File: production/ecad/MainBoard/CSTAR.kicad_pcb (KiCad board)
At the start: 4 copper layers, 152.4 x 152.4 mm, 180 parts, among them IC1 LT8648SEV#PBF, J1 Conn_01x02_Pin, J10 Conn_01x03_Pin, J11 B4B-PH-K-S, J12 B4B-PH-K-S, J13 Conn_01x03_Pin, J13 Conn_01x05_Pin, J14 Conn_01x03_Pin, J15 Conn_01x03_Pin, J16 Conn_01x03_Pin, J17 Ultra_4, J18 Ultra_3, J19 Ultra_2, J2 Conn_01x02_Pin, J20 RX connect, J21 Ultra_1, J22 TX connect, J23 Conn_01x02_Pin, J24 Conn_01x02_Pin, J25 TYPE-C-31-M-12, J26 532610771, J28 532610771, J29 Conn_01x04_Socket, J3 Conn_01x02_Pin, J30 691137710002, J31 TYPE-C-31-M-12, J4 XT60PW-M, J5 Conn_01x02_Pin, J6 Conn_01x02_Pin, J7 532610771, J8 Conn_01x03_Pin, J9 Conn_01x03_Pin, Q1 AO3400A, Q2 AO3400A, Q3 AO3400A, Q4 AO3400A, Q5 AO3400A, Q6 AO3400A, Q7 AO3400A, Q8 IRFHM9331TRPBF, SW1 SW_Push, SW2 SW_Push, SW3 SW_Push, SW4 SW_Push, U1 AZ1117IH-3.3TRG1, U2 DRV8842PWPR, U3 DRV8842PWPR, U4 TXB0104DR, U5 CP2102N-A01-GQFN28, U6 ESP32-WROOM-32UE_M113EH6400UH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, U7 TXB0104DR, U8 CP2102N-A01-GQFN28, U9 ESP32-WROOM-32UE_M113EH6400UH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, X1 B2P-VH, X2 B2P-VH

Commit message: "Layout Routing"
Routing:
- net GND: track 135.7 -> 204.5 mm, vias 36 -> 59
- net EN: track 0.00 -> 36.9 mm
- net +3V3: track 25.7 -> 52.0 mm, vias 2 -> 12
- net RTS: track 0.00 -> 18.3 mm
- net DTR: track 0.00 -> 17.1 mm
- net +12V: track 37.6 -> 53.0 mm, vias 5 -> 9
- net Net-(U3-VCP): track 0.00 -> 14.4 mm
- net Net-(U4-OE): track 0.00 -> 13.8 mm
- net Net-(U3-V3P3OUT): track 0.00 -> 12.1 mm
- net RGB_Red_Control: track 0.00 -> 12.0 mm
- net RGB_Green_Control: track 0.00 -> 11.9 mm
- net /CSTAR-Drive/OUT2_MOTOR_2: track 0.00 -> 9.06 mm
- net /CSTAR-Drive/OUT1_MOTOR_2: track 0.00 -> 8.95 mm
- net Net-(R16-Pad2): track 0.00 -> 8.91 mm
- net IO0: track 0.00 -> 7.18 mm
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
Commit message: "More Layout"
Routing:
- net UART_RXD: track 0.00 -> 71.8 mm, vias 0 -> 2
- net UART_TXD: track 0.00 -> 69.8 mm, vias 0 -> 2
- net 3V_echo_2: track 0.00 -> 40.1 mm, vias 0 -> 2
- net 3V_echo_3: track 0.00 -> 37.8 mm, vias 0 -> 2
- net trig_1: track 0.00 -> 36.4 mm, vias 0 -> 2
- net 3V_echo_1: track 0.00 -> 34.1 mm, vias 0 -> 2
- net 3V_echo_4: track 0.00 -> 30.3 mm, vias 0 -> 2
- net GND: track 204.5 -> 217.3 mm, vias 59 -> 63
- net IO0: track 7.18 -> 18.7 mm
- net IO0_2: track 34.2 -> 41.7 mm
- net EN_2: track 71.4 -> 78.6 mm
- net Net-(U7-OE): track 0.00 -> 6.36 mm
- net EN: track 36.9 -> 41.1 mm
- net +3.3V: track 1.24 -> 4.22 mm, vias 1 -> 3
- net +3V3: track 52.0 -> 54.5 mm, vias 12 -> 14
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
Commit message: "Even more layout"
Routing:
- net Ch.A_MOTOR_2: track 0.00 -> 187.3 mm, vias 0 -> 2
- net Ch.B_MOTOR_2: track 0.00 -> 172.7 mm, vias 0 -> 2
- net IN2_MOTOR_2: track 0.00 -> 140.5 mm, vias 0 -> 2
- net IN1_MOTOR_1: track 0.00 -> 87.6 mm, vias 0 -> 2
- net RST: track 0.00 -> 70.9 mm, vias 0 -> 2
- net GND: track 217.3 -> 277.9 mm, vias 63 -> 83
- net RXD_LIDAR: track 0.00 -> 45.2 mm
- net TXD_LIDAR: track 0.00 -> 45.2 mm
- net trig_2: track 0.00 -> 37.7 mm
- net VBUS_1: track 0.00 -> 33.2 mm, vias 0 -> 2
- net trig_4: track 0.00 -> 30.0 mm, vias 0 -> 2
- net RGB_Blue_Control: track 0.00 -> 29.9 mm, vias 0 -> 2
- net Net-(R21-Pad2): track 0.00 -> 24.4 mm, vias 0 -> 3
- net trig_3: track 0.00 -> 23.2 mm, vias 0 -> 2
- net Net-(R20-Pad2): track 0.00 -> 21.5 mm, vias 0 -> 3
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
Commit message: added gnd to make diff pairs better
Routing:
- added copper zone on In2.Cu, net GND
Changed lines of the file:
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@@
+    )
+  )
+  (zone (net 2) (net_name "GND") (layer "In2.Cu") (hatch edge 0.5)
+    (priority 7)
+    (connect_pads (clearance 0.5))
+    (min_thickness 0.25) (filled_areas_thickness no)
+    (fill yes (thermal_gap 0.5) (thermal_bridge_width 0.5))
+    (polygon
+      (pts
+        (xy 50.8 120.142)
+        (xy 68.58 120.142)
+        (xy 68.58 133.096)
+        (xy 50.8 133.096)
+      )
+    )
+  )
+  (zone (net 2) (net_name "GND") (layer "In2.Cu") (hatch edge 0.5)
+    (priority 6)
+    (connect_pads (clearance 0.5))
+    (min_thickness 0.25) (filled_areas_thickness no)
+    (fill yes (thermal_gap 0.5) (thermal_bridge_width 0.5))
+    (polygon
+      (pts
+        (xy 203.25 110.075)
+        (xy 181.775 110.025)
+        (xy 181.61 89.916)
+        (xy 203.2 89.916)
+      )
     )
   )
@@
         (xy 175.006 65.532)
         (xy 202.946 65.532)
+        (xy 203.3 89.4)
+        (xy 181.15 89.525)
+        (xy 181.125 110.475)
+        (xy 203.045432 110.475176)
         (xy 203.2 180.34)
         (xy 121.92 180.34)
@@
     (polygon
       (pts
+        (xy 50.8 133.35)
+        (xy 68.834 133.35)
+        (xy 68.834 119.888)
+        (xy 50.829297 119.887984)
         (xy 50.8 64.516)
         (xy 79.502 64.262)

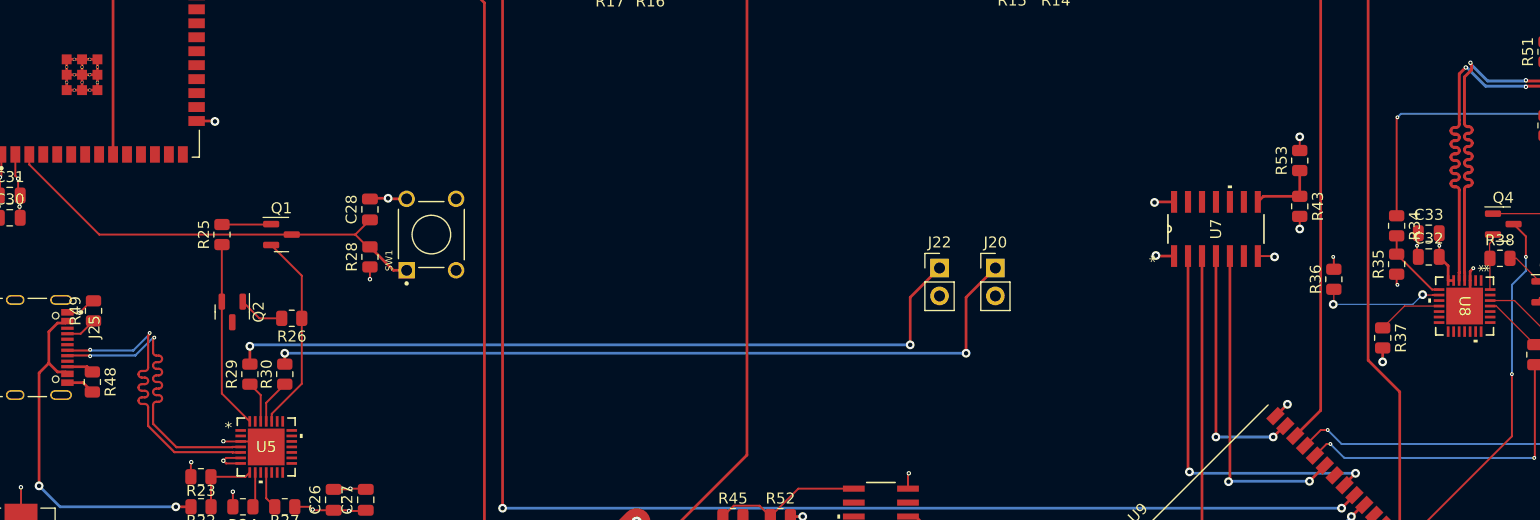
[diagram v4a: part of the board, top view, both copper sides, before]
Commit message: made my diff pairs EVEN BETTER
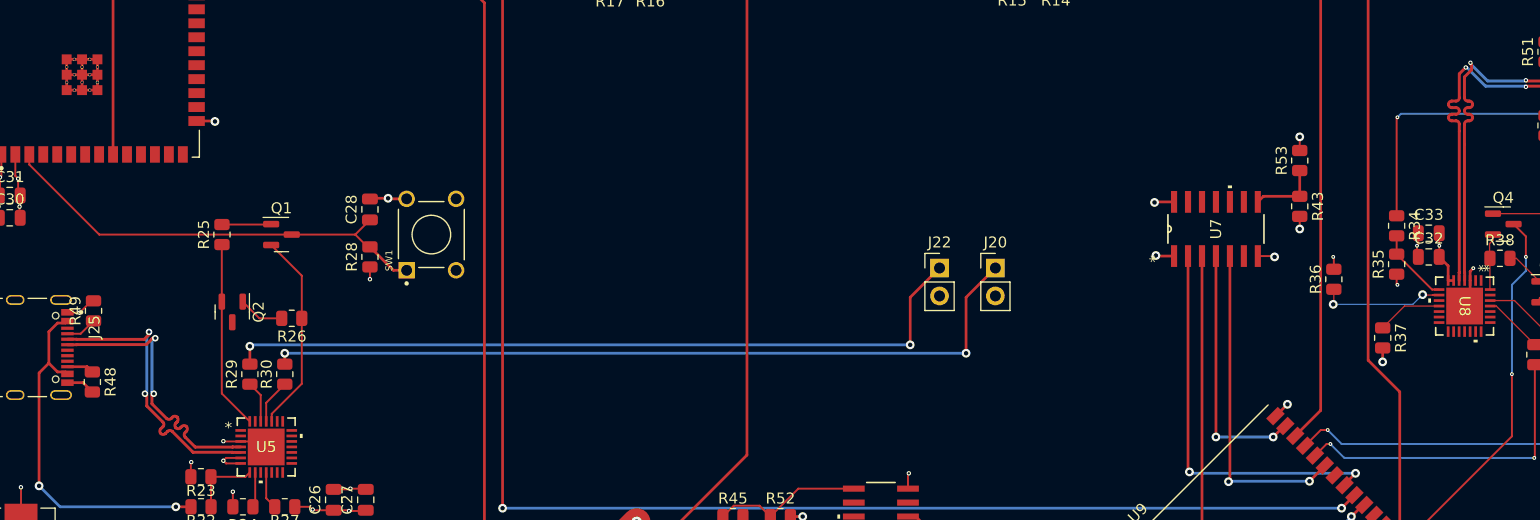
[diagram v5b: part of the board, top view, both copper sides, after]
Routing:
- net USB1_D+: track 29.7 -> 26.5 mm
- net USB1_D-: track 29.8 -> 26.6 mm
- net USB2_D+: track 37.9 -> 35.5 mm
- net USB2_D-: track 38.9 -> 36.9 mm

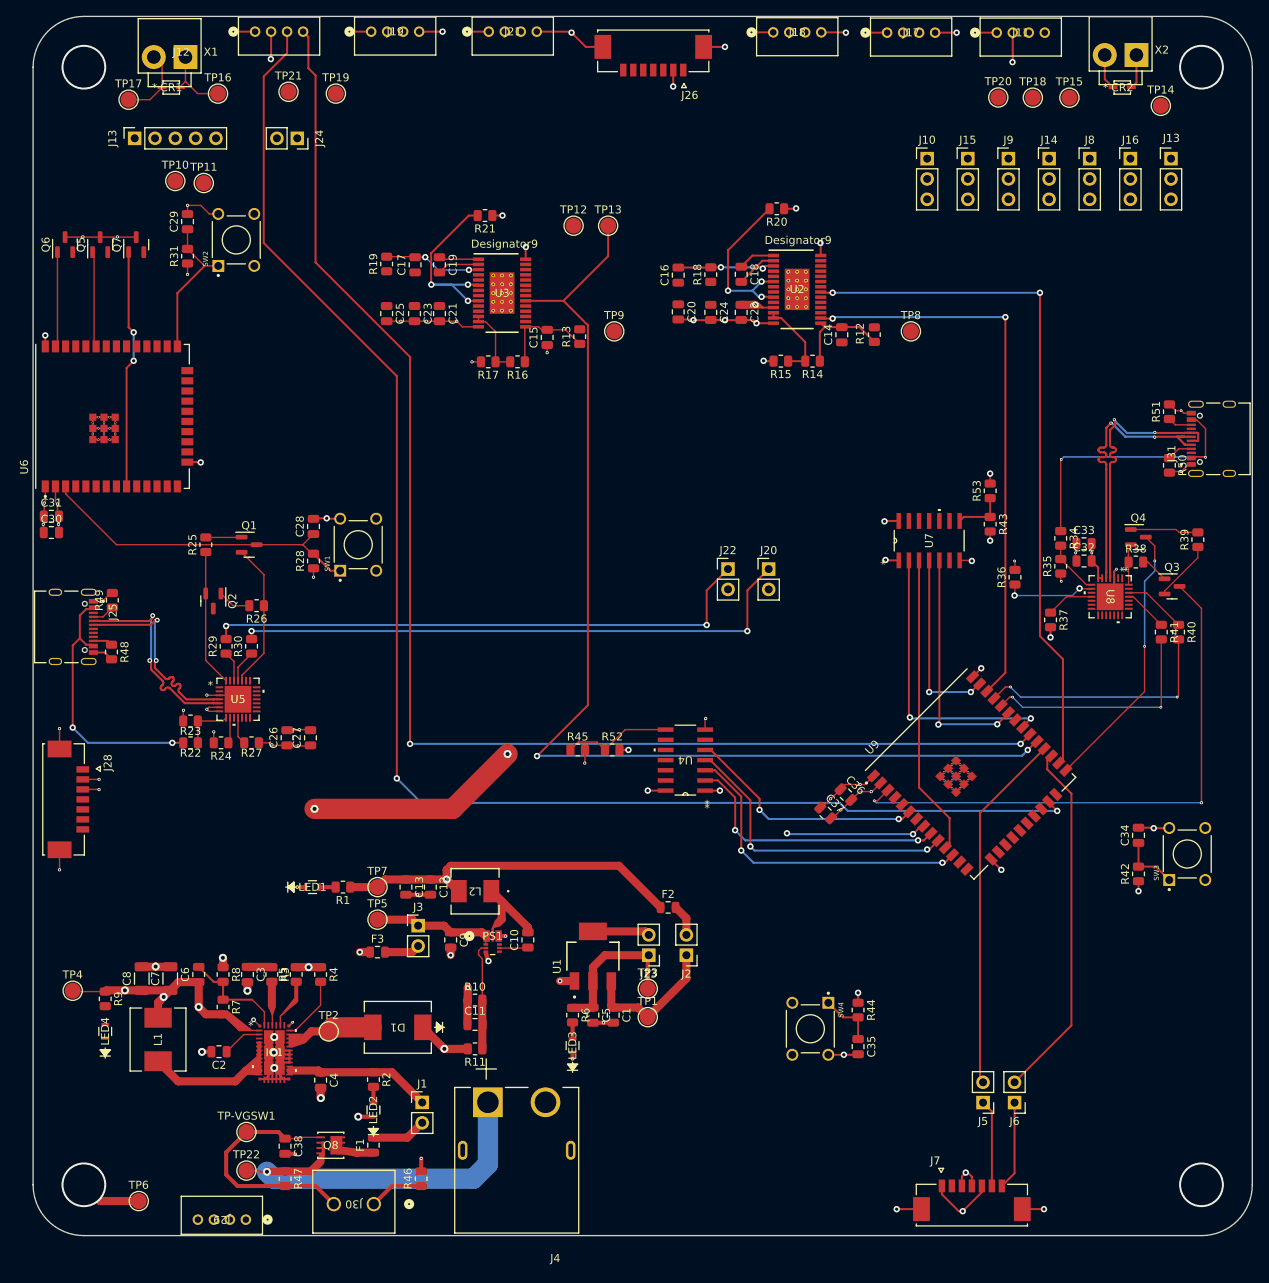
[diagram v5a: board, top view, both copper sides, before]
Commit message: "Routed Current Controllers"
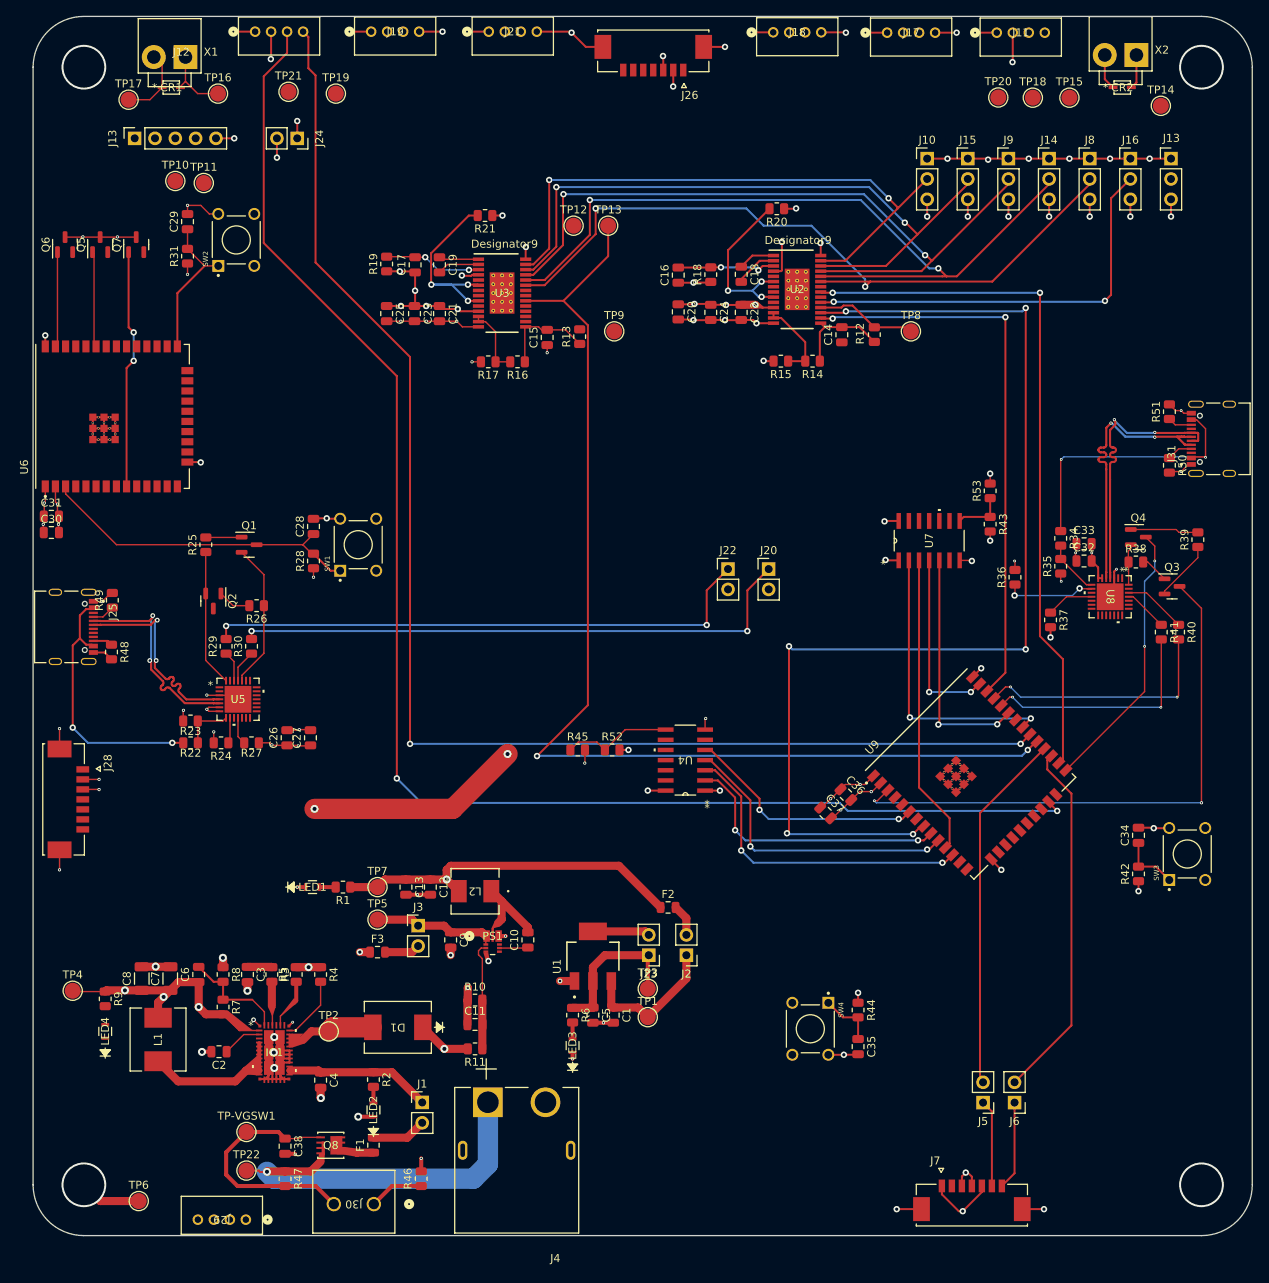
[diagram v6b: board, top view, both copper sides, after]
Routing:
- net SCL: track 17.6 -> 139.3 mm, vias 2 -> 6
- net /CSTAR-Drive/I1: track 0.00 -> 97.2 mm, vias 0 -> 2
- net /CSTAR-Drive/I0: track 0.00 -> 93.1 mm, vias 0 -> 2
- net /CSTAR-Drive/I2: track 0.00 -> 90.7 mm, vias 0 -> 2
- net /CSTAR-Drive/I3: track 0.00 -> 83.3 mm, vias 0 -> 2
- net /CSTAR-Drive/I4: track 0.00 -> 75.0 mm, vias 0 -> 2
- net /CSTAR-Drive/nDECAY: track 0.00 -> 52.2 mm, vias 0 -> 2
- net +12V: track 37.9 -> 78.2 mm, vias 5 -> 16
- net +3V3: track 54.5 -> 86.9 mm, vias 14 -> 21
- net GND: track 277.9 -> 297.7 mm, vias 83 -> 92
- net nFAULT_MOTOR_1: track 0.00 -> 12.7 mm

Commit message: "Better Manhattan"
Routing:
- net nFAULT_MOTOR_2: track 0.00 -> 130.0 mm, vias 0 -> 6
- net IN2_MOTOR_1: track 0.00 -> 93.2 mm, vias 0 -> 2
- net I2S_CLK: track 0.00 -> 88.3 mm, vias 0 -> 3
- net I2S_D2: track 0.00 -> 86.4 mm, vias 0 -> 2
- net nFAULT_MOTOR_1: track 12.7 -> 93.3 mm, vias 0 -> 8
- net I2S_CMD: track 0.00 -> 74.9 mm, vias 0 -> 3
- net I2S_D0: track 0.00 -> 71.1 mm, vias 0 -> 2
- net /CSTAR-Drive/I1: track 97.2 -> 40.1 mm
- net /CSTAR-Drive/I2: track 90.7 -> 34.4 mm
- net /CSTAR-Drive/I3: track 83.3 -> 28.5 mm
- net /CSTAR-Drive/I4: track 75.0 -> 22.4 mm
- net /CSTAR-Drive/I0: track 93.1 -> 54.7 mm
- net Ch.A_MOTOR_2: track 187.3 -> 191.2 mm
- net 3V_echo_4: track 30.3 -> 33.9 mm, vias 2 -> 4
- net Ch.B_MOTOR_2: track 172.7 -> 176.2 mm
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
